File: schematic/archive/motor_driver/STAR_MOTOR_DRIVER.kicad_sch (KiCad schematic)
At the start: 46 parts, among them J1 6120XX21621_61200821621, J10 B6B-XH-A, J11 B6B-XH-A, J12 B6B-XH-A, J2 6120XX21621_61200621621, J3 B6B-XH-A, J4 6120XX21621_61200821621, J5 6120XX21621_61200821621, J6 6120XX21621_61200821621, J7 1017491, U1 DRV8243SQDGQRQ1 (S-Variant), U2 DRV8243SQDGQRQ1 (S-Variant), U3 DRV8243SQDGQRQ1 (S-Variant), U4 DRV8243SQDGQRQ1 (S-Variant)

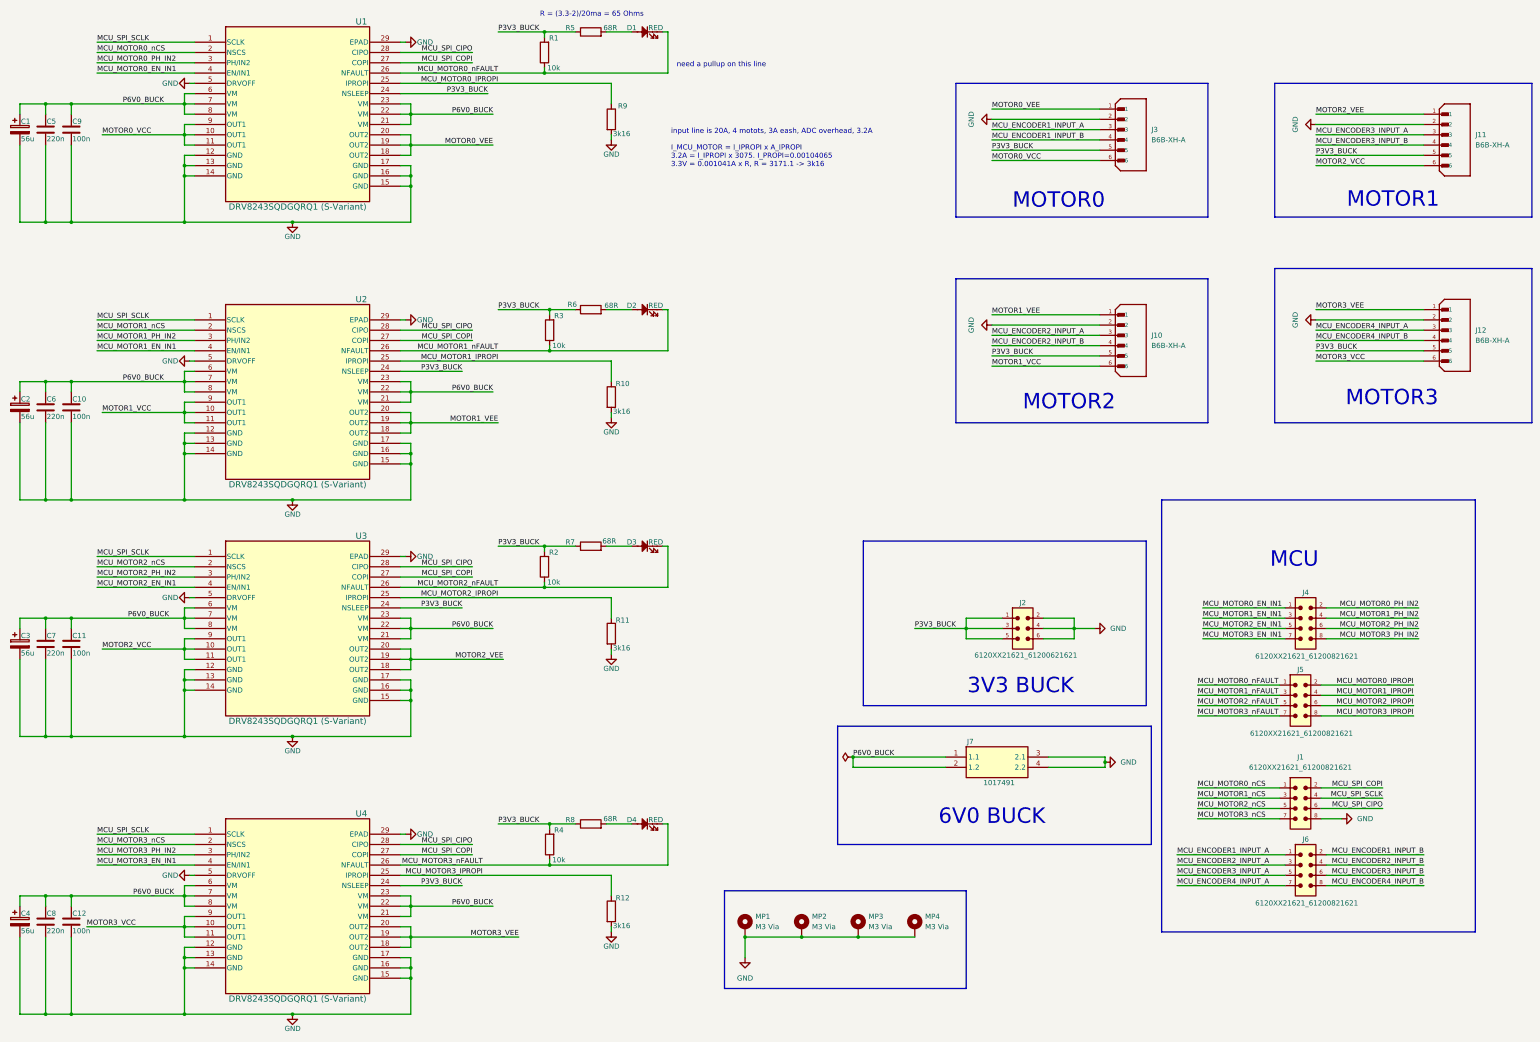
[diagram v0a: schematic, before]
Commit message: Finished Power Board, working on BMS, moved Motor Driver to archive, added Motor Driver to MCU
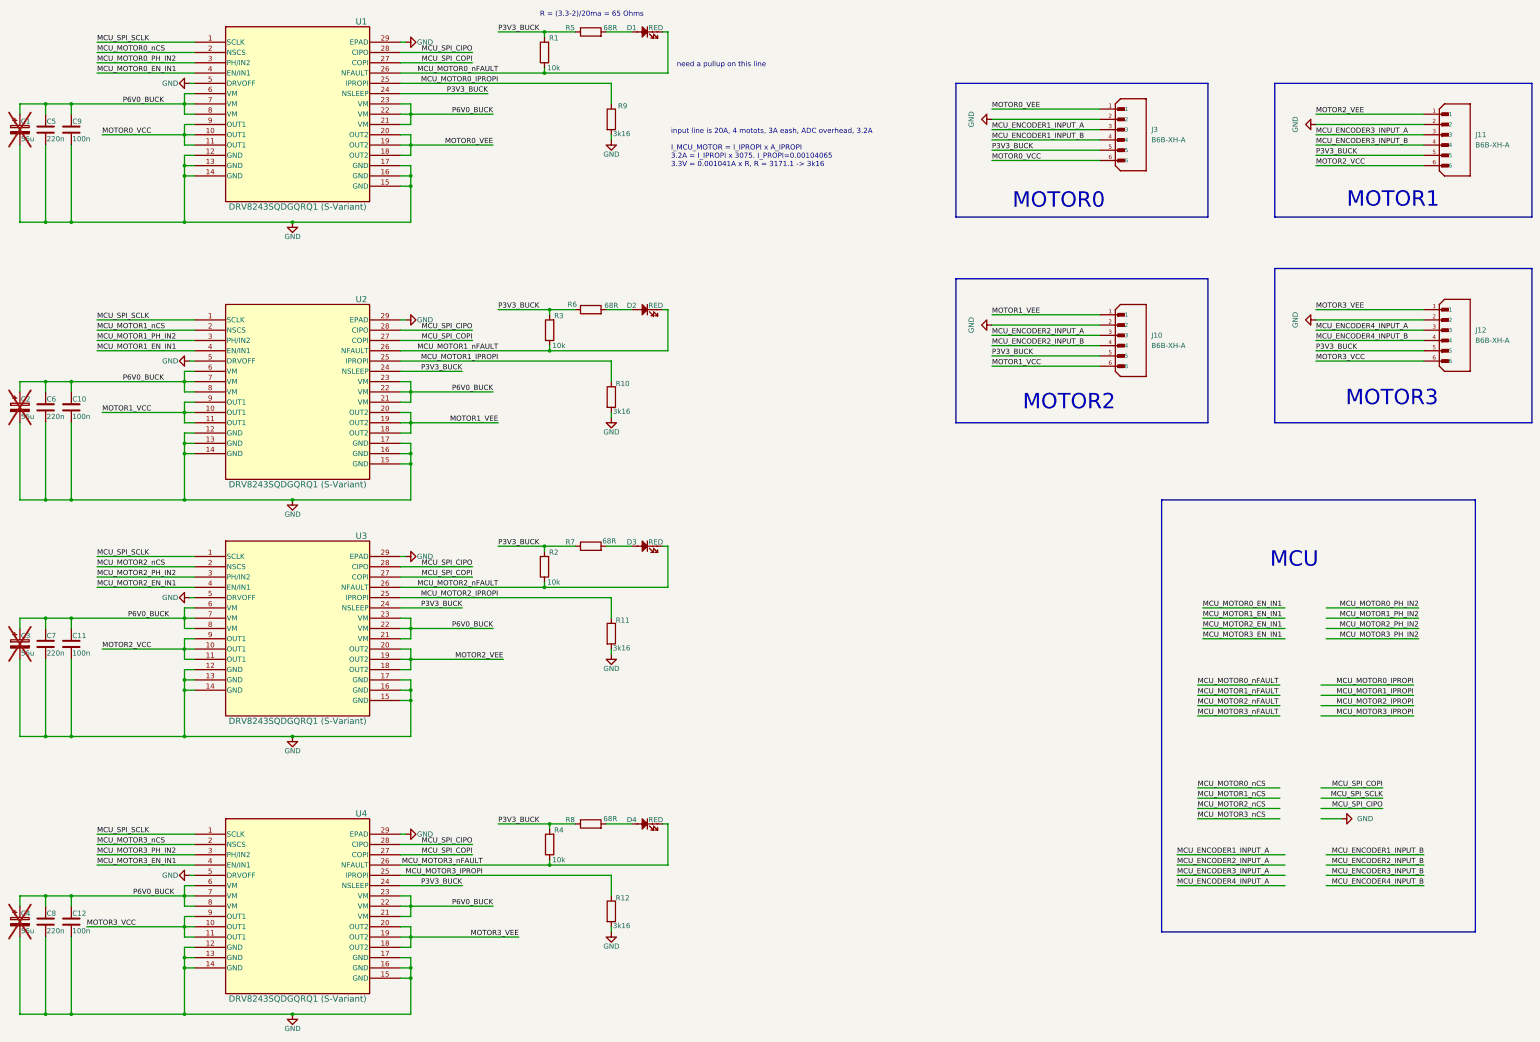
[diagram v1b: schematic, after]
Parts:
- removed J1, J4, J5, J6: 6120XX21621_61200821621, 61200821621:61200821621, symbol 61200821621:6120XX21621_61200821621
- removed J2: 6120XX21621_61200621621, 61200621621:61200621621, symbol 61200621621:6120XX21621_61200621621
- removed J7: 1017491, 1017491, symbol 1017491:1017491
- removed MP1, MP2, MP3, MP4: M3 Via, MountingHole:MountingHole_3.2mm_M3_Pad_Via, symbol Mechanical:MountingHole_Pad
- C1, C2, C3, C4: now not fitted
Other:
- note removed: "3V3 BUCK"
- note removed: "6V0 BUCK"
